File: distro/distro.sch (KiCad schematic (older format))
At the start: 17 parts, among them K1 CONN_3, P10 CONN_2, P11 CONN_2, P12 CONN_2, P13 CONN_2, P3 CONN_2, P4 CONN_2, P5 CONN_2, P6 CONN_2, P8 CONN_2, P9 CONN_2

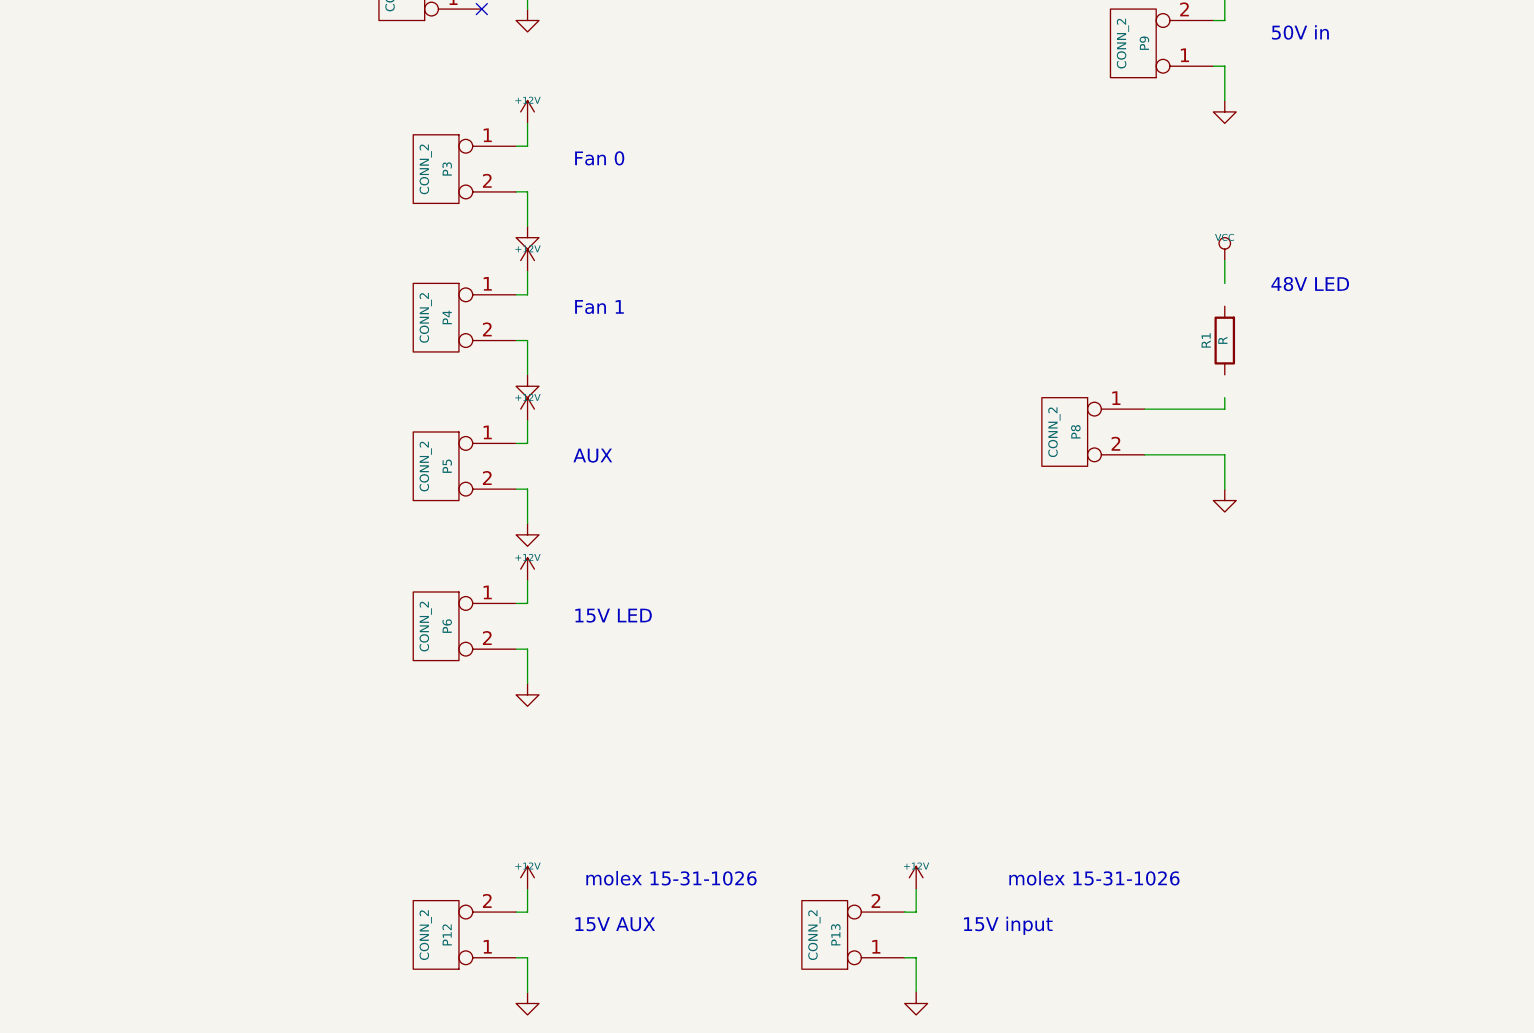
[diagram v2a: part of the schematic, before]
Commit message: component footprint changes to simplify bom
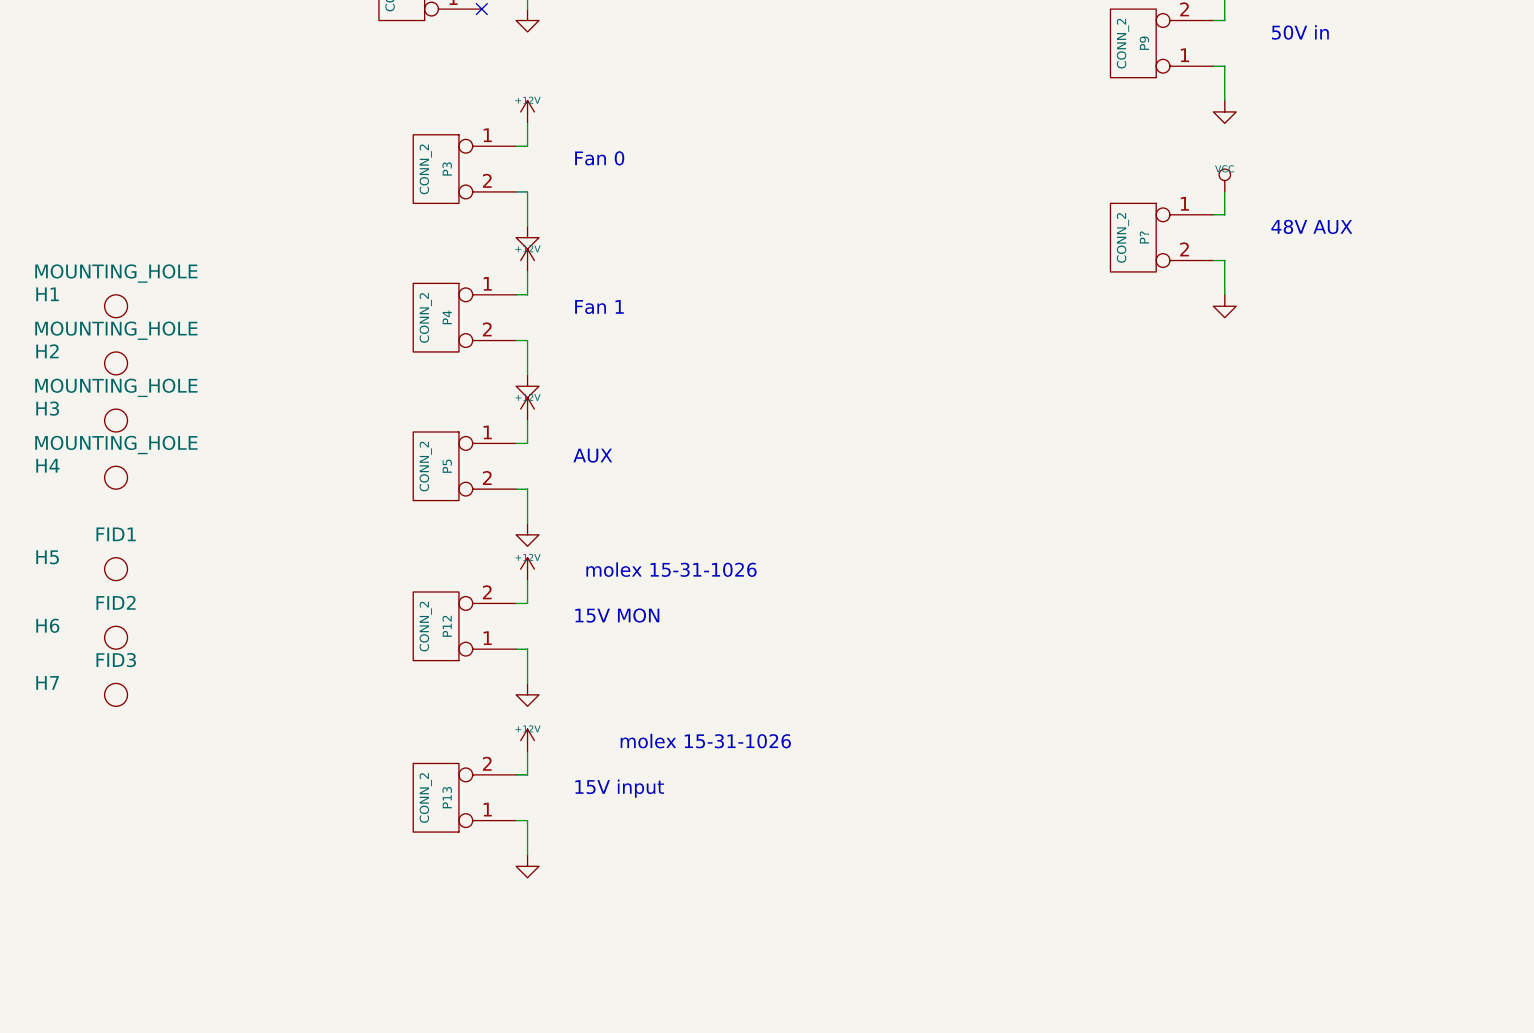
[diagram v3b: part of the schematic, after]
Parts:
- removed P6, P8: CONN_2, Connect:PINHEAD1-2, symbol CONN_2
- removed R1: R, SMD_Packages:SMD-0805, symbol R
- added H1, H2, H3, H4: MOUNTING_HOLE, Mounting_Holes:MountingHole_6-5mm, symbol MOUNTING_HOLE
- added H5: FID1, sdtransmitter:FID_1MM, symbol MOUNTING_HOLE
- added H6: FID2, sdtransmitter:FID_1MM, symbol MOUNTING_HOLE
- added H7: FID3, sdtransmitter:FID_1MM, symbol MOUNTING_HOLE
- added P?: CONN_2, sdtransmitter:0740991003, symbol CONN_2
- K1: footprint Connect:PINHEAD1-3 -> sdtransmitter:0740991003
- P3, P4, P5: footprint Connect:PINHEAD1-2 -> sdtransmitter:0740991003
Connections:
- wire segments 55 -> 50
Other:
- note added: "15V MON"
- note added: "48V AUX"
- note removed: "15V AUX"
- note removed: "15V LED"
- note removed: "48V LED"
- moved on the sheet: P12, P13

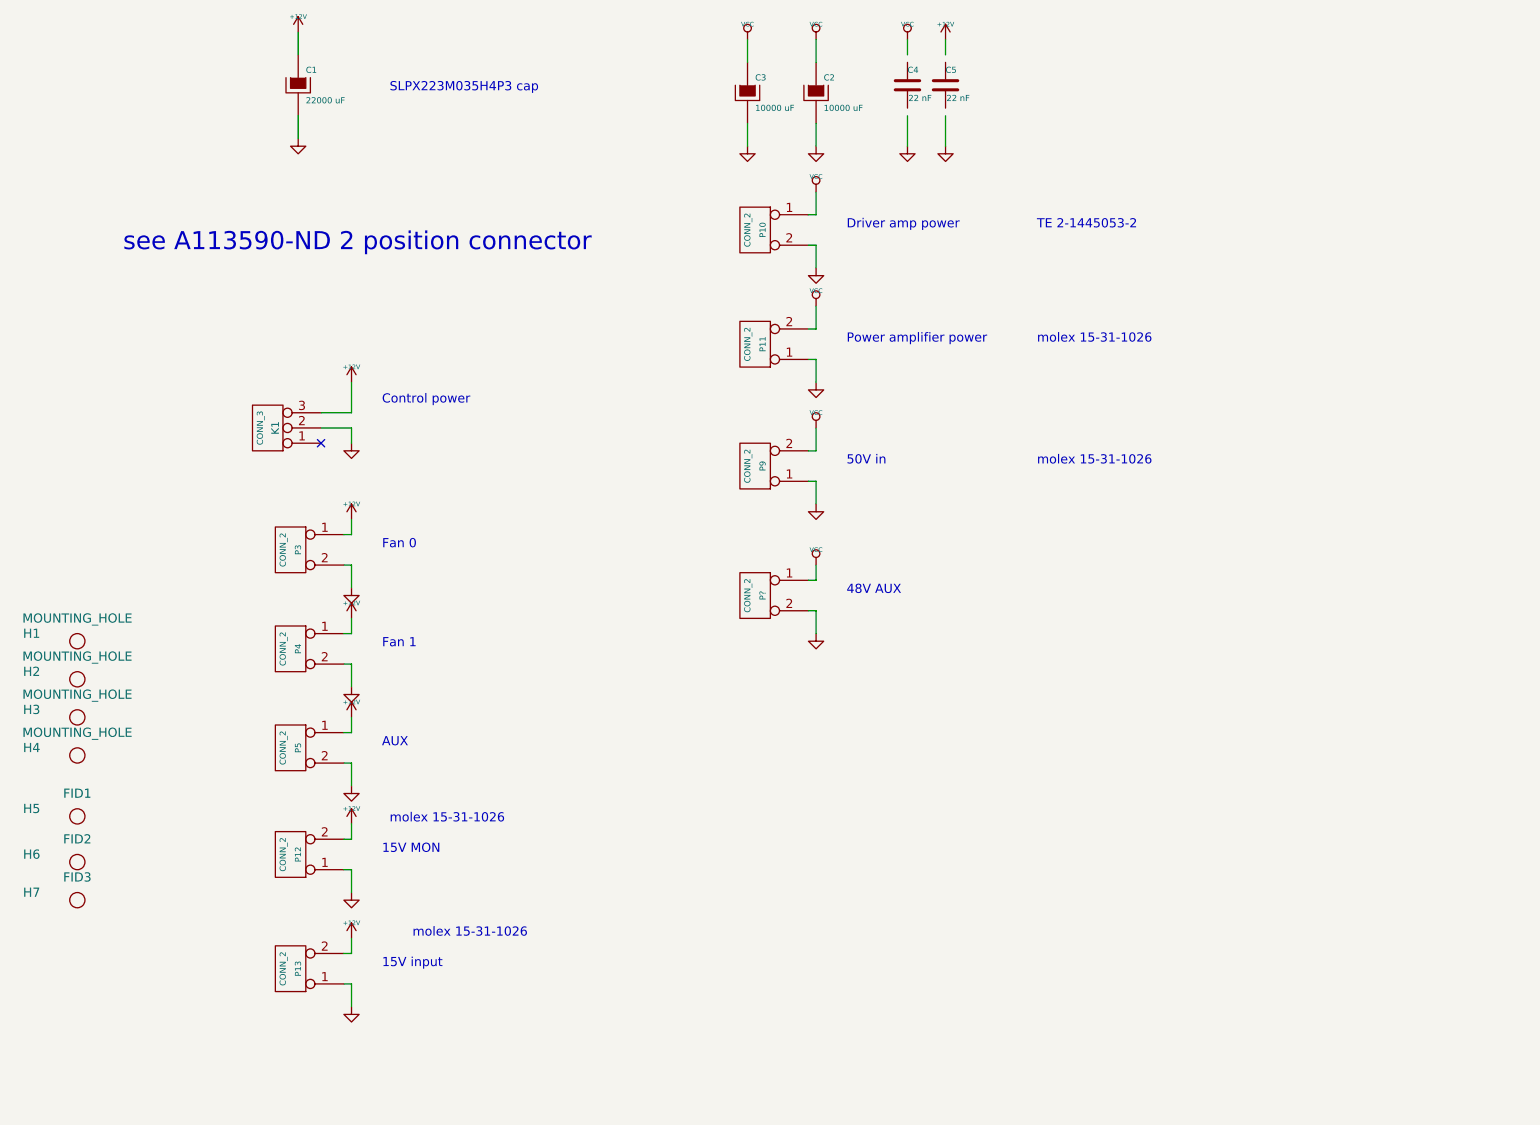
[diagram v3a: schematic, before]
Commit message: shrank power distro board for mounting on plate, updated transmitter plate drawings
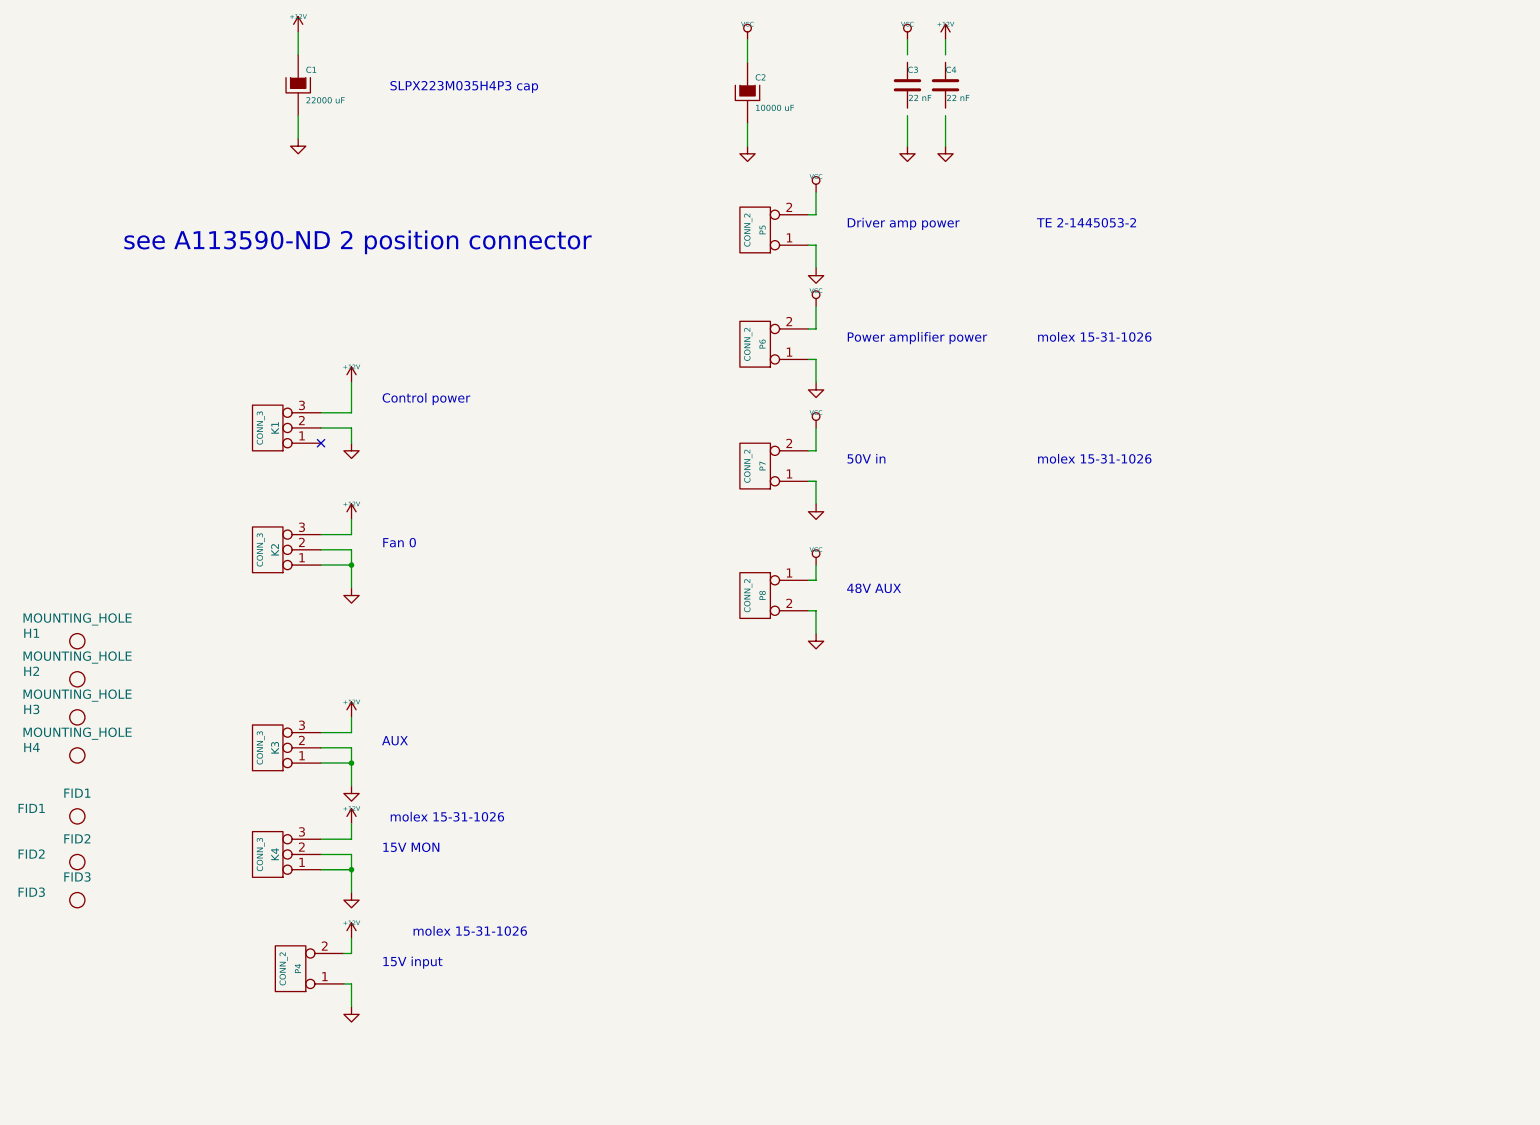
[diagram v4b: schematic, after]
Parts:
- removed C2: 10000 uF, Capacitors_ThroughHole:Capacitor35x51RM10, symbol CAPAPOL
- removed P12: CONN_2, local:0015311026, symbol CONN_2
- removed P3, P4, P5: CONN_2, sdtransmitter:0740991003, symbol CONN_2
- added K2, K3, K4: CONN_3, sdtransmitter:0740991003, symbol CONN_3
- gave numbers to parts that had none: 1
- renumbered C3 to C2, C4 to C3, C5 to C4, H5 to FID1, H6 to FID2, H7 to FID3, P13 to P4, P10 to P5, P11 to P6, P9 to P7
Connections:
- wire segments 50 -> 47
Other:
- note removed: "Fan 1"

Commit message: DFM changes after last protoype rev
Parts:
- removed P8: CONN_2, sdtransmitter:0740991003, symbol CONN_2
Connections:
- wire segments 47 -> 43
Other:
- note removed: "48V AUX"
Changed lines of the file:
@@
-$EndComp
-$Comp
-L CONN_2 P8
-U 1 1 54D9632B
-P 5700 4350
-F 0 "P8" V 5650 4350 40  0000 C CNN
-F 1 "CONN_2" V 5750 4350 40  0000 C CNN
-F 2 "sdtransmitter:0740991003" H 5700 4350 60  0001 C CNN
-F 3 "" H 5700 4350 60  0000 C CNN
-	1    5700 4350
-	-1   0    0    -1
-$EndComp
-$Comp
-L GND #PWR024
-U 1 1 54D96331
-P 6100 4600
-F 0 "#PWR024" H 6100 4600 30  0001 C CNN
-F 1 "GND" H 6100 4530 30  0001 C CNN
-F 2 "" H 6100 4600 60  0000 C CNN
-F 3 "" H 6100 4600 60  0000 C CNN
-	1    6100 4600
-	1    0    0    -1
-$EndComp
-Text Notes 6300 4350 0    60   ~ 0
-48V AUX
-$Comp
-L VCC #PWR025
-U 1 1 54D9633C
-P 6100 4150
-F 0 "#PWR025" H 6100 4250 30  0001 C CNN
-F 1 "VCC" H 6100 4250 30  0000 C CNN
-F 2 "" H 6100 4150 60  0000 C CNN
-F 3 "" H 6100 4150 60  0000 C CNN
-	1    6100 4150
-	1    0    0    -1
 $EndComp
 $Comp
@@
 	3050 6900 3050 7050
 Wire Wire Line
-	6050 4250 6100 4250
-Wire Wire Line
-	6100 4250 6100 4150
-Wire Wire Line
-	6050 4450 6100 4450
-Wire Wire Line
-	6100 4450 6100 4600
-Wire Wire Line
 	3050 4050 3050 4300

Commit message: added fields for manufacturer/distributor part number to schematic
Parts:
- H1, H2, H3, H4: footprint Mounting_Holes:MountingHole_6-5mm -> Mounting_Holes:MountingHole_3-5mm
- P5: footprint local:2-1445053-2 -> local:0015311026
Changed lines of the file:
@@
 F 0 "P5" V 5650 1950 40  0000 C CNN
 F 1 "CONN_2" V 5750 1950 40  0000 C CNN
-F 2 "local:2-1445053-2" H 5700 1950 60  0001 C CNN
+F 2 "local:0015311026" H 5700 1950 60  0001 C CNN
 F 3 "" H 5700 1950 60  0000 C CNN
 	1    5700 1950
@@
 F 0 "H1" H 950 4700 60  0000 C CNN
 F 1 "MOUNTING_HOLE" H 1250 4800 60  0000 C CNN
-F 2 "Mounting_Holes:MountingHole_6-5mm" H 1250 4650 60  0001 C CNN
+F 2 "Mounting_Holes:MountingHole_3-5mm" H 1250 4650 60  0001 C CNN
 F 3 "" H 1250 4650 60  0000 C CNN
 	1    1250 4650
@@
 F 0 "H2" H 950 4950 60  0000 C CNN
 F 1 "MOUNTING_HOLE" H 1250 5050 60  0000 C CNN
-F 2 "Mounting_Holes:MountingHole_6-5mm" H 1250 4900 60  0001 C CNN
+F 2 "Mounting_Holes:MountingHole_3-5mm" H 1250 4900 60  0001 C CNN
 F 3 "" H 1250 4900 60  0000 C CNN
 	1    1250 4900
@@
 F 0 "H3" H 950 5200 60  0000 C CNN
 F 1 "MOUNTING_HOLE" H 1250 5300 60  0000 C CNN
-F 2 "Mounting_Holes:MountingHole_6-5mm" H 1250 5150 60  0001 C CNN
+F 2 "Mounting_Holes:MountingHole_3-5mm" H 1250 5150 60  0001 C CNN
 F 3 "" H 1250 5150 60  0000 C CNN
 	1    1250 5150
@@
 F 0 "H4" H 950 5450 60  0000 C CNN
 F 1 "MOUNTING_HOLE" H 1250 5550 60  0000 C CNN
-F 2 "Mounting_Holes:MountingHole_6-5mm" H 1250 5400 60  0001 C CNN
+F 2 "Mounting_Holes:MountingHole_3-5mm" H 1250 5400 60  0001 C CNN
 F 3 "" H 1250 5400 60  0000 C CNN
 	1    1250 5400
@@
 	2850 4150 3050 4150
 $Comp
-L GND #PWR026
+L GND #PWR024
 U 1 1 5408CDDD
 P 3050 4300
-F 0 "#PWR026" H 3050 4300 30  0001 C CNN
+F 0 "#PWR024" H 3050 4300 30  0001 C CNN
 F 1 "GND" H 3050 4230 30  0001 C CNN
 F 2 "" H 3050 4300 60  0000 C CNN
